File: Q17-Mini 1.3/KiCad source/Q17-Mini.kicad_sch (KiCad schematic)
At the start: 86 parts, among them J1 Input, J2-1 SPK+, J2-2 SPK-, J3-1 V+, J3-2 GND, J3-3 V-, Q1 IRF610, Q10 KSA992, Q11 ZVP2106A, Q12 BD139, Q13 IRF610, Q14 IRF9610, Q15 FQA46N15, Q16 FQA36P15, Q2 KSA992, Q3 KSC1845, Q4 IRF9610, Q5 FQP3P20, Q6 FQP3N30, Q7 KSC1845, Q8 ZVN4206AV, Q9 ZVP2106A, U1 OPA1641

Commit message: Update diagram for Q17-Mini 1.3
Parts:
- J1: Part# Terminal Block KF128 5mm 2P -> Terminal Block KF127 5mm 2P
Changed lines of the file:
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@@
   (title_block
     (title "Q17-Mini Amplifier")
-    (date "2022-08-31")
-    (rev "1.3.8")
+    (date "2022-09-01")
+    (rev "1.3.9")
     (company "by eng. Tiberiu Vicol")
     (comment 1 "Modified by Stef for the Q17-Mini project")
@@
       (effects (font (size 1.27 1.27)) hide)
     )
-    (property "Part#" "Terminal Block KF128 5mm 2P" (id 4) (at 17.78 76.2 0)
-      (effects (font (size 1.27 1.27)) hide)
-    )
+    (property "Part#" "Terminal Block KF127 5mm 2P" (id 4) (at 17.78 76.2 0)
+      (effects (font (size 1.27 1.27)) hide)
+    )

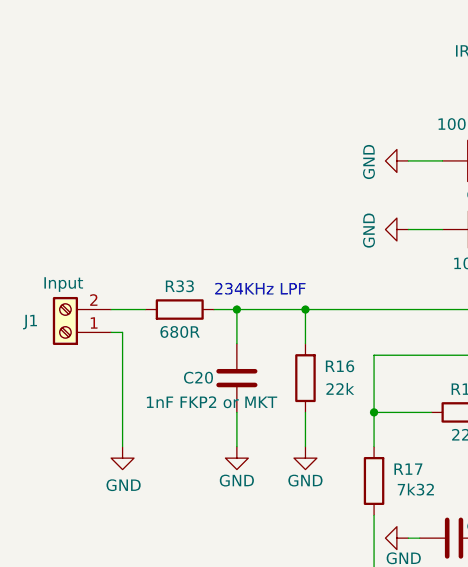
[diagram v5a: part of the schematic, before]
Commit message: Update Input_connector_mix_ footprint files
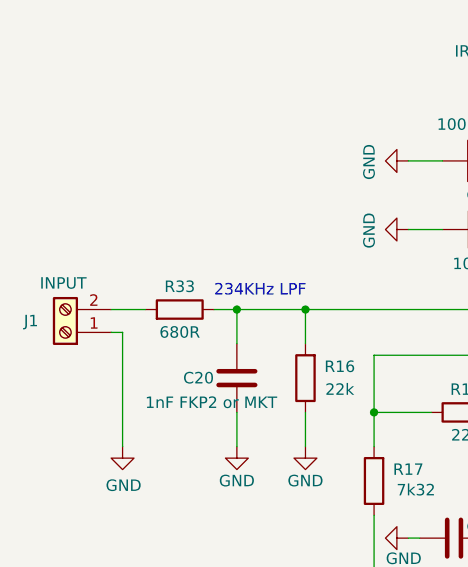
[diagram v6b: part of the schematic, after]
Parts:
- J1: value Input -> INPUT
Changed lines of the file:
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@@
     (in_bom yes) (on_board yes)
     (property "Reference" "J1" (id 0) (at 13.97 74.93 0))
-    (property "Value" "Input" (id 1) (at 17.526 70.7475 0))
+    (property "Value" "INPUT" (id 1) (at 17.526 70.7475 0))
     (property "Footprint" "TerminalBlock_Phoenix:TerminalBlock_Phoenix_PT-1,5-2-5.0-H_1x02_P5.00mm_Horizontal" (id 2) (at 17.78 76.2 0)
       (effects (font (size 1.27 1.27)) hide)
@@
     )
     (path "/849e771a-b2fa-4ff5-b7a4-96512b8b3abe"
-      (reference "J1") (unit 1) (value "Input") (footprint "TerminalBlock_Phoenix:TerminalBlock_Phoenix_PT-1,5-2-5.0-H_1x02_P5.00mm_Horizontal")
+      (reference "J1") (unit 1) (value "INPUT") (footprint "TerminalBlock_Phoenix:TerminalBlock_Phoenix_PT-1,5-2-5.0-H_1x02_P5.00mm_Horizontal")
     )
     (path "/e013bf34-127e-4c4d-b8a5-cc04b193e5e8"

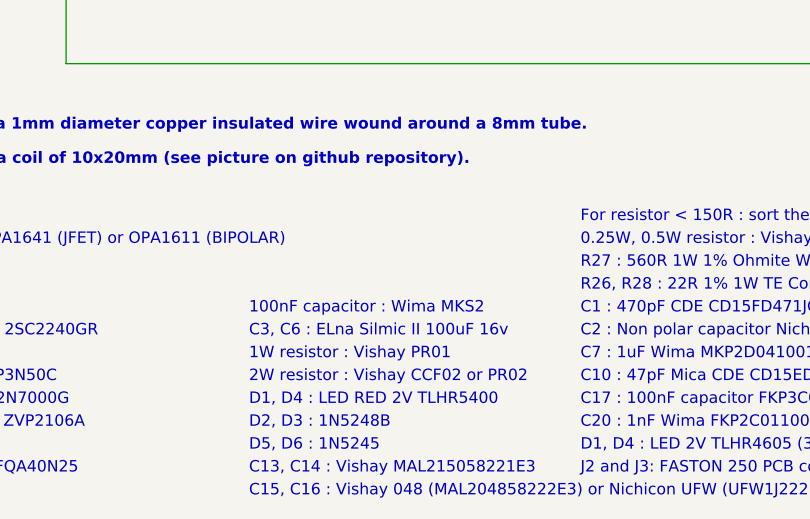
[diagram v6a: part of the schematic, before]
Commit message: Update diagram for Q17-Mini 1.3
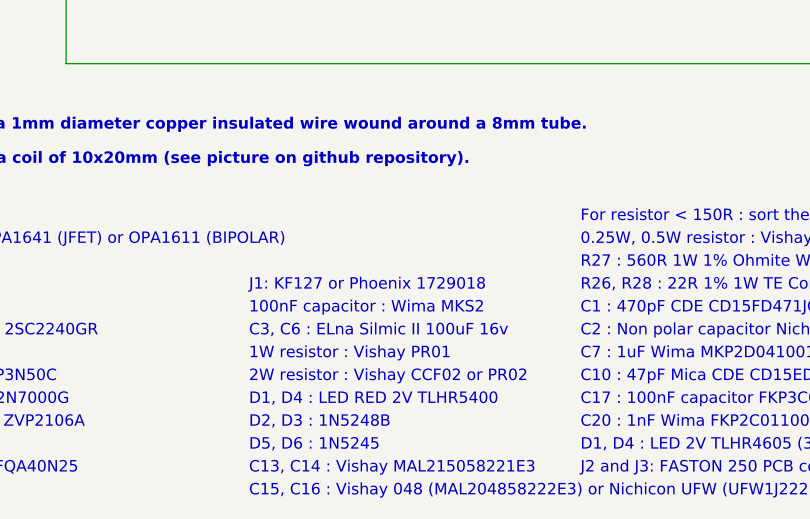
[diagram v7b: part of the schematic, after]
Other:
- note added: "J1: KF127 or Phoenix 1729018"
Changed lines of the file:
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@@
   (title_block
     (title "Q17-Mini Amplifier")
-    (date "2022-09-01")
+    (date "2022-09-03")
     (rev "1.3.9")
     (company "by eng. Tiberiu Vicol")
@@
     (effects (font (size 1.27 1.27)) (justify left bottom))
   )
+  (text "J1: KF127 or Phoenix 1729018" (at 59.69 173.99 0)
+    (effects (font (size 1.27 1.27)) (justify left bottom))
+  )

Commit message: Update diagram for Q17-Mini 1.3
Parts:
- C13: Part# Vishay MAL215058221E3 -> MAL215058221E3
- C14: Part# Vishat MAL215058221E3 -> MAL215058221E3
- C3, C6: Part# Elna Silmic II RFS-16V101MH3#5 -> RFS-16V101MH3#5
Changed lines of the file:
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@@
   (title_block
     (title "Q17-Mini Amplifier")
-    (date "2022-09-03")
+    (date "2022-09-07")
     (rev "1.3.9")
     (company "by eng. Tiberiu Vicol")
@@
       (effects (font (size 1.27 1.27)) hide)
     )
-    (property "Part#" "Elna Silmic II RFS-16V101MH3#5" (id 4) (at 63.5 107.95 90)
+    (property "Part#" "RFS-16V101MH3#5" (id 4) (at 63.5 107.95 90)
       (effects (font (size 1.27 1.27)) hide)
     )
@@
       (effects (font (size 1.27 1.27)) hide)
     )
-    (property "Part#" "Vishay MAL215058221E3" (id 4) (at 205.74 40.64 0)
+    (property "Part#" "MAL215058221E3" (id 4) (at 205.74 40.64 0)
       (effects (font (size 1.27 1.27)) hide)
     )
@@
       (effects (font (size 1.27 1.27)) hide)
     )
-    (property "Part#" "Vishat MAL215058221E3" (id 4) (at 205.74 125.73 0)
+    (property "Part#" "MAL215058221E3" (id 4) (at 205.74 125.73 0)
       (effects (font (size 1.27 1.27)) hide)
     )
@@
       (effects (font (size 1.27 1.27)) hide)
     )
-    (property "Part#" "Elna Silmic II RFS-16V101MH3#5" (id 4) (at 63.5 57.15 90)
-      (effects (font (size 1.27 1.27)) hide)
-    )
+    (property "Part#" "RFS-16V101MH3#5" (id 4) (at 63.5 57.15 90)
+      (effects (font (size 1.27 1.27)) hide)
+    )
